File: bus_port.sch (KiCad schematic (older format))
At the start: 3 parts

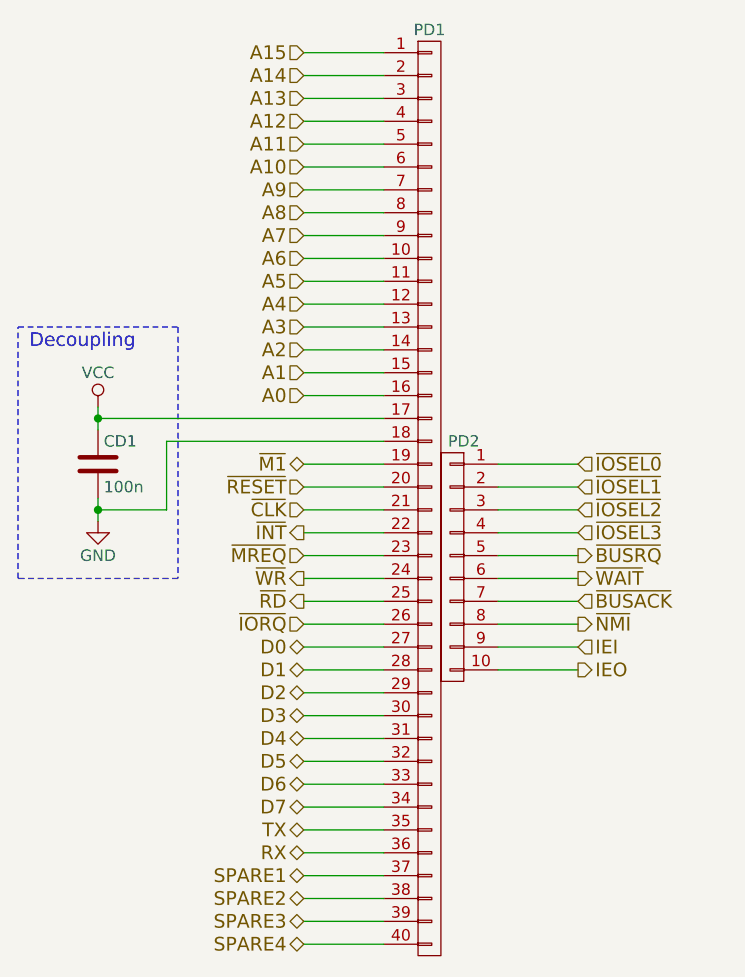
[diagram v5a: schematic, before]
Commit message: Added logo schematic elements and new logo for bottom side.
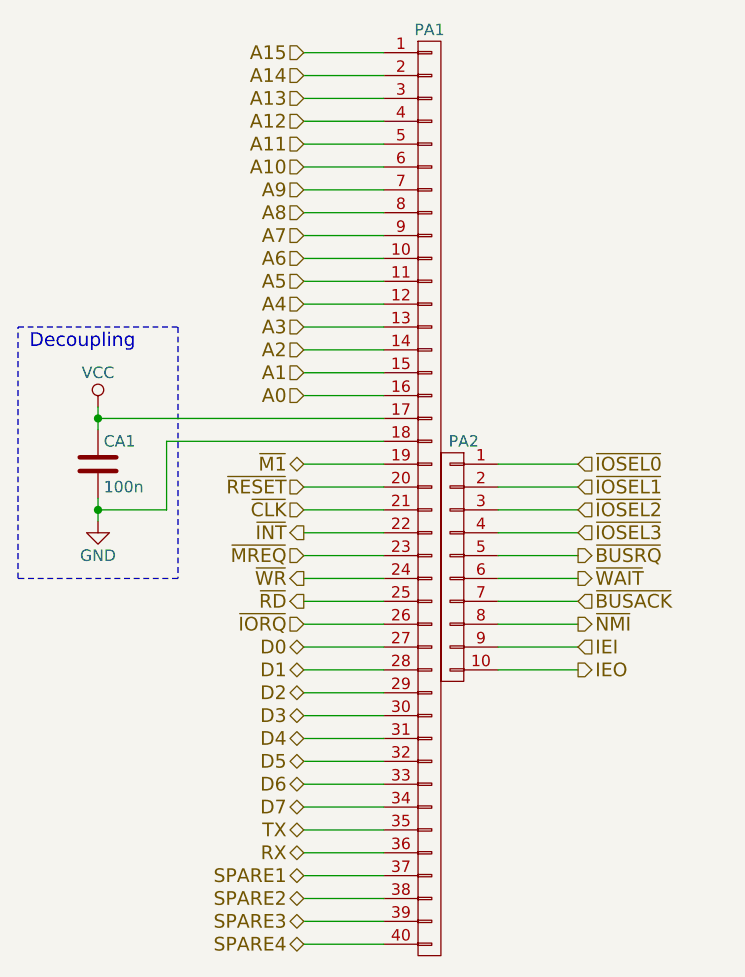
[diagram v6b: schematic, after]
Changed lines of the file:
@@
 LIBS:atf16v8cv
 LIBS:62256
+LIBS:mcp2221a
 LIBS:z80-cache
 EELAYER 25 0
@@
 AR Path="/577F17CE/5797AD5E/5780CE22" Ref="CD1"  Part="1"
 AR Path="/577F17CE/5798778E/5780CE22" Ref="CE1"  Part="1"
-F 0 "CD1" H 3025 4650 50  0000 L CNN
+F 0 "CA1" H 3025 4650 50  0000 L CNN
 F 1 "100n" H 3025 4450 50  0000 L CNN
 F 2 "Capacitors_ThroughHole:C_Rect_L4_W2.5_P2.5" H 3038 4400 50  0001 C CNN
@@
 AR Path="/577F17CE/5797AD5E/579E12E5" Ref="PD1"  Part="1"
 AR Path="/577F17CE/5798778E/579E12E5" Ref="PE1"  Part="1"
-F 0 "PD1" H 4450 6750 50  0000 C CNN
+F 0 "PA1" H 4450 6750 50  0000 C CNN
 F 1 "CONN_01X40" V 4550 6400 50  0001 C CNN
 F 2 "Socket_Strips:Socket_Strip_Straight_1x40" H 4450 4700 50  0001 C CNN
@@
 AR Path="/577F17CE/5797AC61/57B9EC3D" Ref="PC2"  Part="1"
 AR Path="/577F17CE/5797AD5E/57B9EC3D" Ref="PD2"  Part="1"
-F 0 "PD2" H 4500 5550 50  0000 C CNN
+F 0 "PA2" H 4500 5550 50  0000 C CNN
 F 1 "CONN_01X10" V 4650 5000 50  0001 C CNN
 F 2 "Socket_Strips:Socket_Strip_Straight_1x10" H 4550 5000 50  0001 C CNN

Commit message: * fixed DRC errors on pin 1 of Px2 connectors. * fixed unconnected ground pin issue of GAL. * added 8DIP and 14DIP oscillator block footprint. * updated bottom silkscreen. * added via stitching in a few places for better GND net. * routed the reset and oscillator circuits. * Design passes KiCAD DRC.
!! This is NRC016 RC1 !!
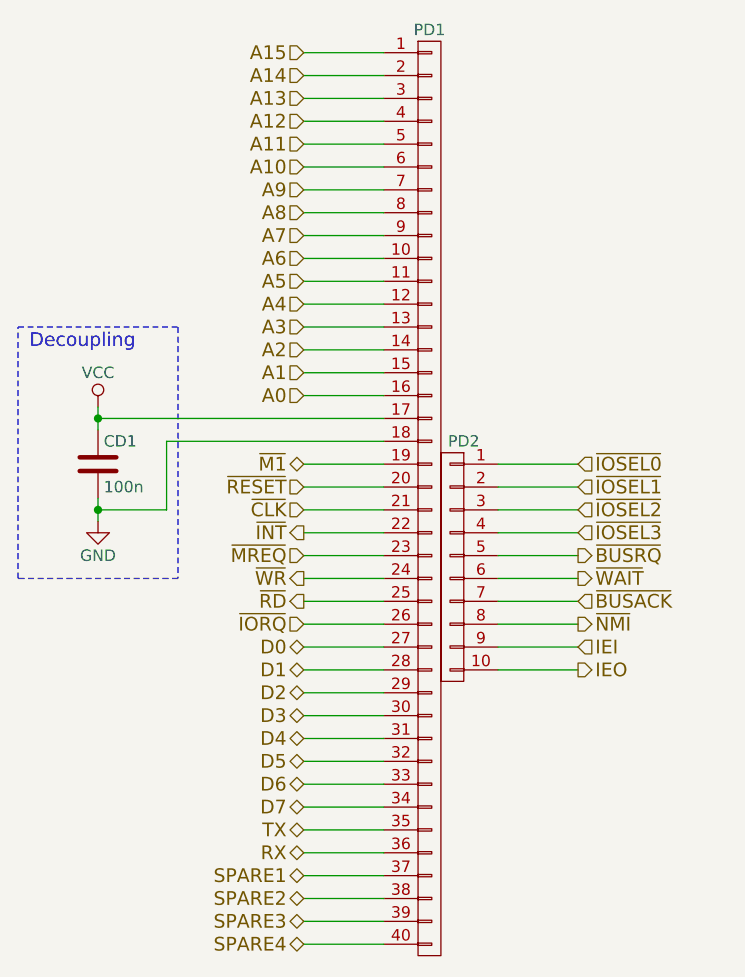
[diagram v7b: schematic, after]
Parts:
- PA2: footprint Socket_Strips:Socket_Strip_Straight_1x10 -> nrc2016:Socket_Strip_Straight_1x10_NRC2016
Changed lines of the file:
@@
 AR Path="/577F17CE/5797AD5E/5780CE22" Ref="CD1"  Part="1"
 AR Path="/577F17CE/5798778E/5780CE22" Ref="CE1"  Part="1"
-F 0 "CA1" H 3025 4650 50  0000 L CNN
+F 0 "CD1" H 3025 4650 50  0000 L CNN
 F 1 "100n" H 3025 4450 50  0000 L CNN
 F 2 "Capacitors_ThroughHole:C_Rect_L4_W2.5_P2.5" H 3038 4400 50  0001 C CNN
@@
 AR Path="/577F17CE/5797AD5E/579E12E5" Ref="PD1"  Part="1"
 AR Path="/577F17CE/5798778E/579E12E5" Ref="PE1"  Part="1"
-F 0 "PA1" H 4450 6750 50  0000 C CNN
+F 0 "PD1" H 4450 6750 50  0000 C CNN
 F 1 "CONN_01X40" V 4550 6400 50  0001 C CNN
 F 2 "Socket_Strips:Socket_Strip_Straight_1x40" H 4450 4700 50  0001 C CNN
@@
 AR Path="/577F17CE/5797AC61/57B9EC3D" Ref="PC2"  Part="1"
 AR Path="/577F17CE/5797AD5E/57B9EC3D" Ref="PD2"  Part="1"
-F 0 "PA2" H 4500 5550 50  0000 C CNN
+F 0 "PD2" H 4500 5550 50  0000 C CNN
 F 1 "CONN_01X10" V 4650 5000 50  0001 C CNN
-F 2 "Socket_Strips:Socket_Strip_Straight_1x10" H 4550 5000 50  0001 C CNN
+F 2 "nrc2016:Socket_Strip_Straight_1x10_NRC2016" H 4550 5000 50  0001 C CNN
 F 3 "" H 4550 5000 50  0000 C CNN
 	1    4550 5000

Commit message: Fix screw up with VCC and GND on rc2014 slots.
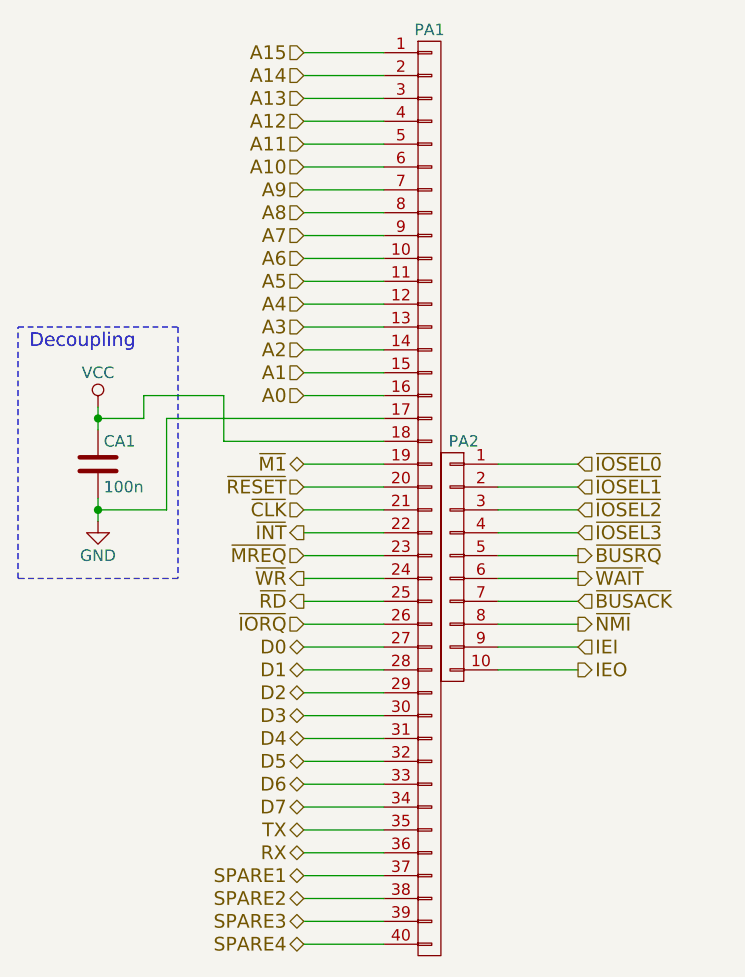
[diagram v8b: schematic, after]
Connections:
- net GND: now also PA1.17 (P17); no longer PA1.18 (P18)
- net VCC: now also PA1.18 (P18); no longer PA1.17 (P17)
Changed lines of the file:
@@
 Comment4 ""
 $EndDescr
-Wire Wire Line
-	3000 4350 4250 4350
-Wire Wire Line
-	3300 4450 4250 4450
 $Comp
 L C CA1
@@
 AR Path="/577F17CE/5797AD5E/5780CE22" Ref="CD1"  Part="1"
 AR Path="/577F17CE/5798778E/5780CE22" Ref="CE1"  Part="1"
-F 0 "CD1" H 3025 4650 50  0000 L CNN
+F 0 "CA1" H 3025 4650 50  0000 L CNN
 F 1 "100n" H 3025 4450 50  0000 L CNN
 F 2 "Capacitors_ThroughHole:C_Rect_L4_W2.5_P2.5" H 3038 4400 50  0001 C CNN
@@
 AR Path="/577F17CE/5797AD5E/5780D6F2" Ref="#PWR031"  Part="1"
 AR Path="/577F17CE/5798778E/5780D6F2" Ref="#PWR036"  Part="1"
-F 0 "#PWR031" H 3000 4150 50  0001 C CNN
+F 0 "#PWR025" H 3000 4150 50  0001 C CNN
 F 1 "VCC" H 3000 4450 50  0000 C CNN
 F 2 "" H 3000 4300 50  0000 C CNN
@@
 AR Path="/577F17CE/5797AD5E/5780D706" Ref="#PWR032"  Part="1"
 AR Path="/577F17CE/5798778E/5780D706" Ref="#PWR037"  Part="1"
-F 0 "#PWR032" H 3000 4550 50  0001 C CNN
+F 0 "#PWR026" H 3000 4550 50  0001 C CNN
 F 1 "GND" H 3000 4650 50  0000 C CNN
 F 2 "" H 3000 4800 50  0000 C CNN
@@
 	2650 5050 2650 3950
 Wire Wire Line
-	3300 4450 3300 4750
+	3300 4350 3300 4750
 Connection ~ 3000 4350
 Wire Wire Line
@@
 AR Path="/577F17CE/5797AD5E/579E12E5" Ref="PD1"  Part="1"
 AR Path="/577F17CE/5798778E/579E12E5" Ref="PE1"  Part="1"
-F 0 "PD1" H 4450 6750 50  0000 C CNN
+F 0 "PA1" H 4450 6750 50  0000 C CNN
 F 1 "CONN_01X40" V 4550 6400 50  0001 C CNN
 F 2 "Socket_Strips:Socket_Strip_Straight_1x40" H 4450 4700 50  0001 C CNN
@@
 AR Path="/577F17CE/5797AC61/57B9EC3D" Ref="PC2"  Part="1"
 AR Path="/577F17CE/5797AD5E/57B9EC3D" Ref="PD2"  Part="1"
-F 0 "PD2" H 4500 5550 50  0000 C CNN
+F 0 "PA2" H 4500 5550 50  0000 C CNN
 F 1 "CONN_01X10" V 4650 5000 50  0001 C CNN
 F 2 "nrc2016:Socket_Strip_Straight_1x10_NRC2016" H 4550 5000 50  0001 C CNN
@@
 Wire Wire Line
 	4750 5450 5100 5450
+Wire Wire Line
+	3300 4350 4250 4350
+Wire Wire Line
+	3000 4350 3200 4350
+Wire Wire Line
+	3200 4350 3200 4250
+Wire Wire Line
+	3200 4250 3550 4250
+Wire Wire Line
+	3550 4250 3550 4450
+Wire Wire Line
+	3550 4450 4250 4450
 $EndSCHEMATC
